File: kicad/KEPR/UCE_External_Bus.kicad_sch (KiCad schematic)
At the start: 5 parts, among them J4 Conn_02x40_Odd_Even, J5 Conn_02x40_Odd_Even, J6 Conn_02x40_Odd_Even, J7 Conn_02x08_Odd_Even, J8 Conn_01x08_Pin

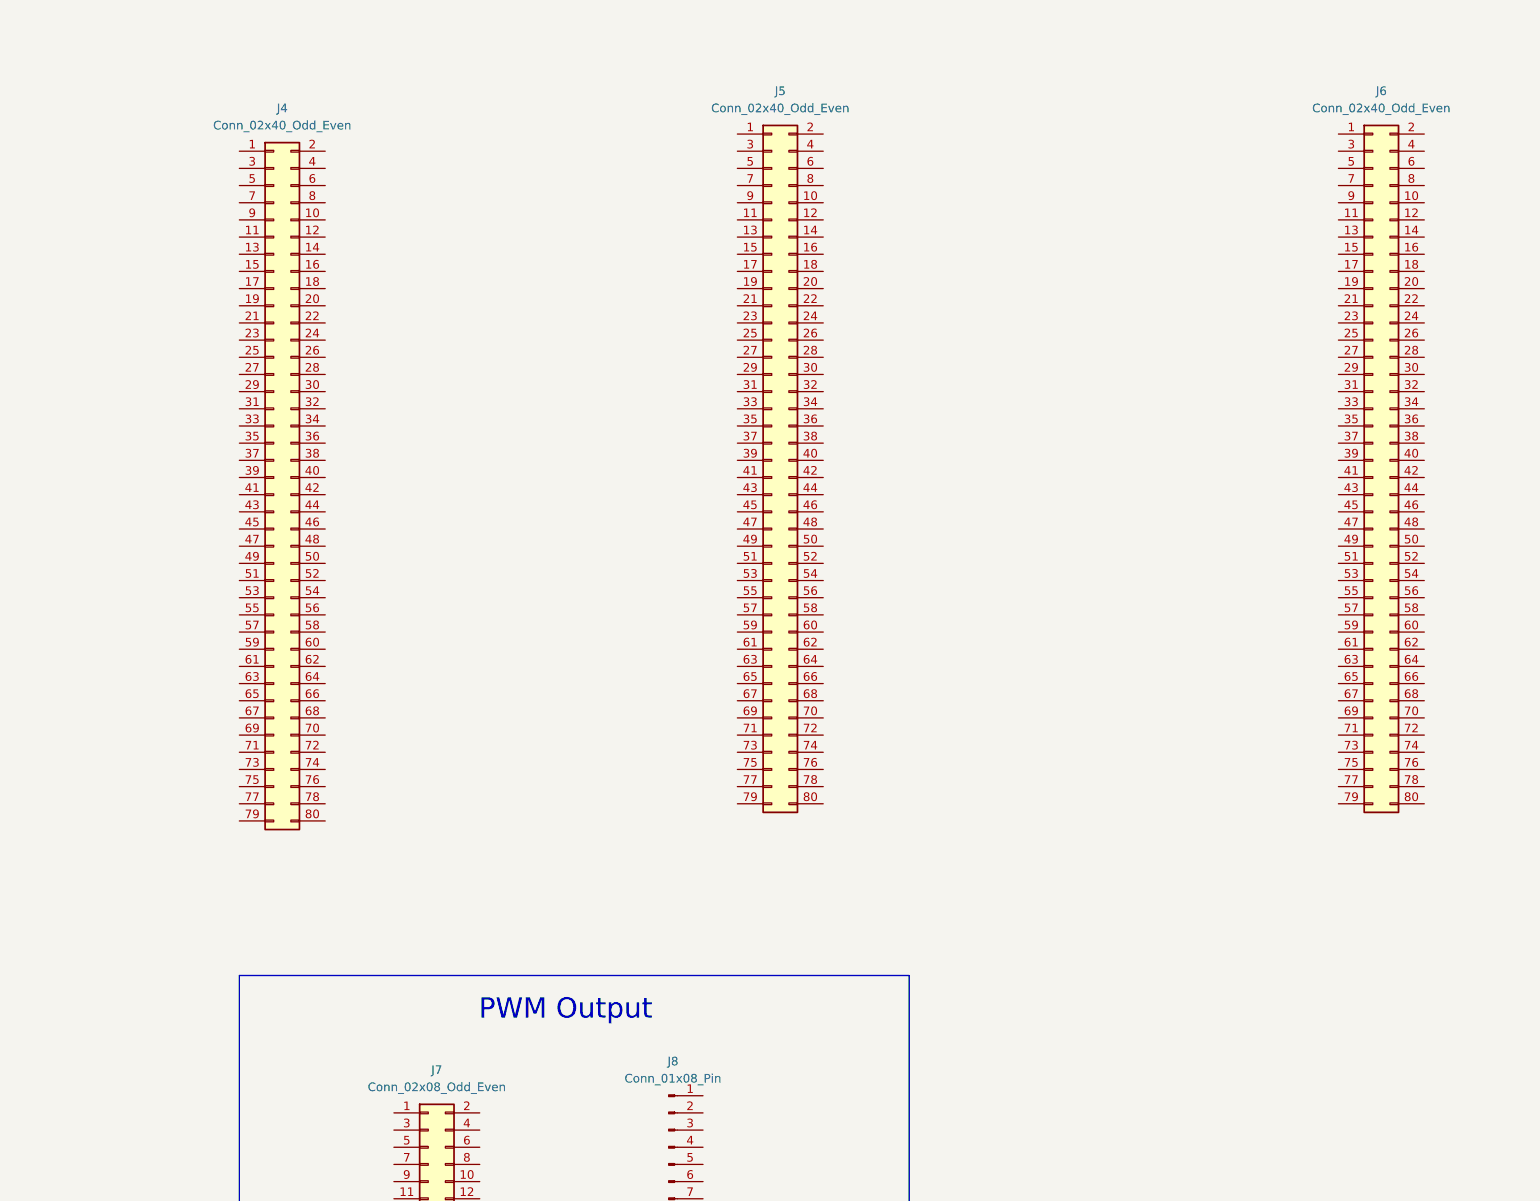
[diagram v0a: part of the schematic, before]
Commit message: Adicinado o barramento externo
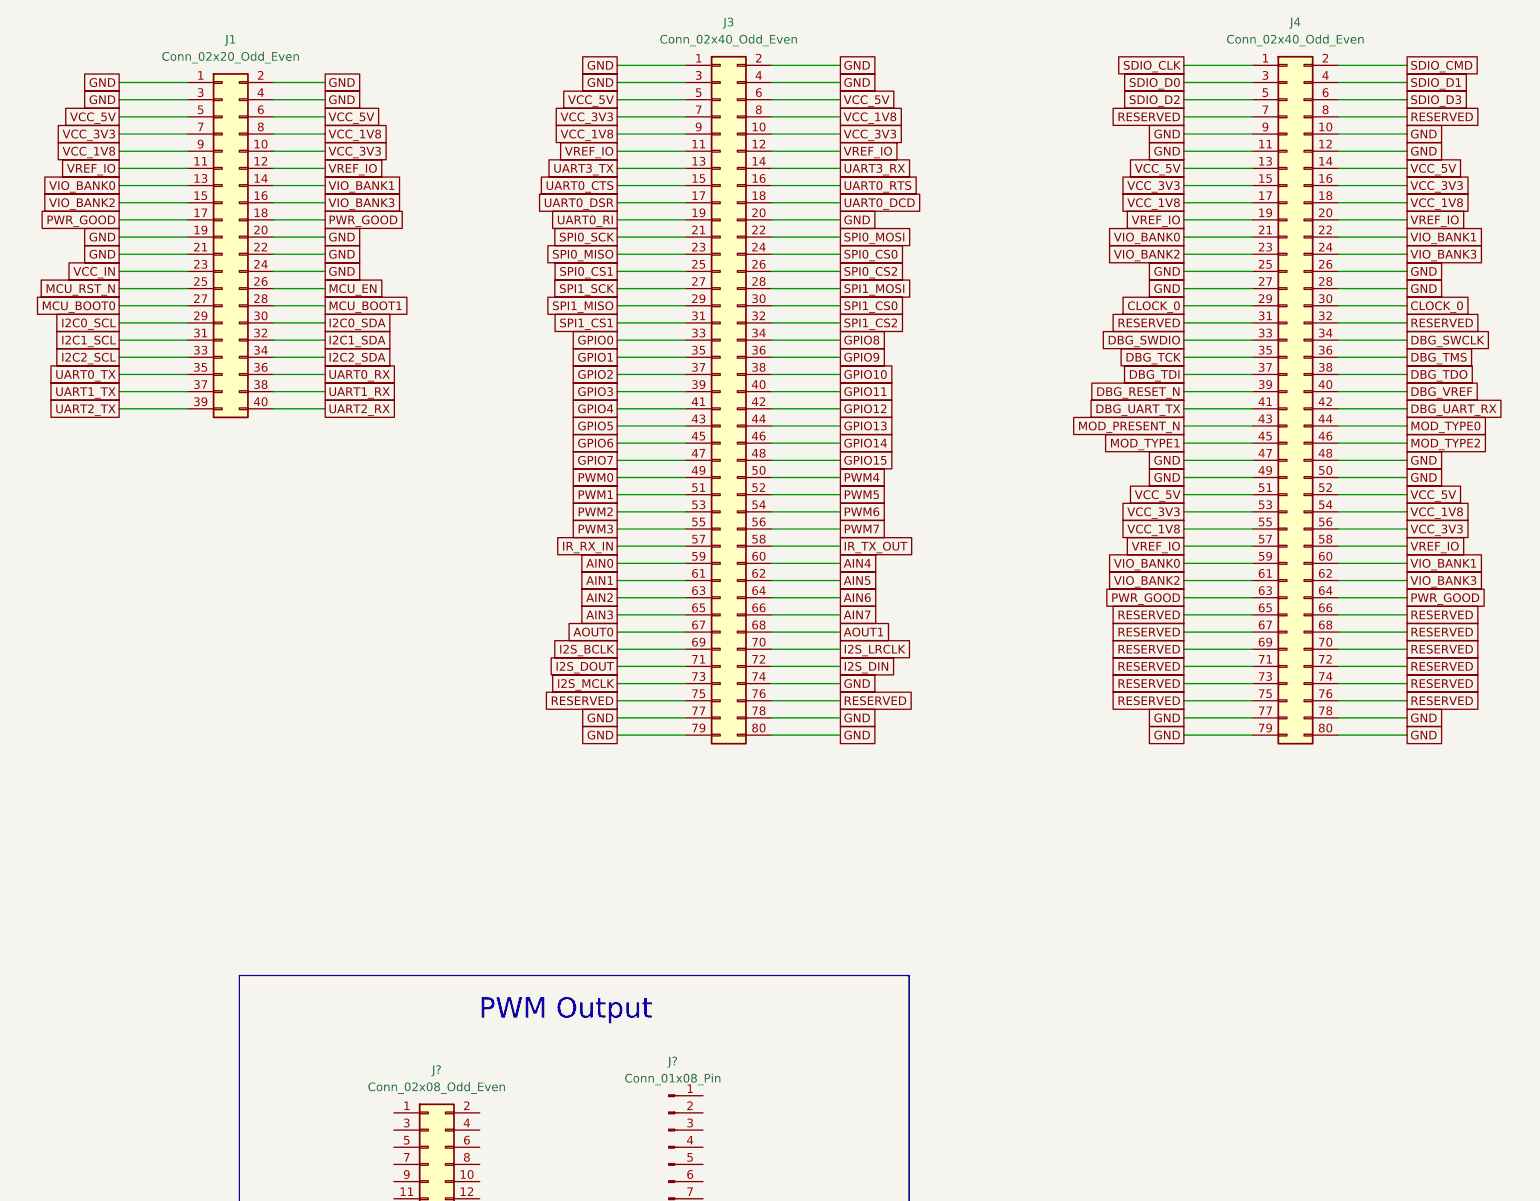
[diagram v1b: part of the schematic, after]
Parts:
- removed J5, J6: Conn_02x40_Odd_Even, symbol Connector_Generic:Conn_02x40_Odd_Even
- added J1: Conn_02x20_Odd_Even, symbol Connector_Generic:Conn_02x20_Odd_Even
- added J3: Conn_02x40_Odd_Even, symbol Connector_Generic:Conn_02x40_Odd_Even
- renumbered J8 to J?, J7 to J?
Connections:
- net SDIO_CLK: now reaches J4.1 (Pin_1)
- net GND: now reaches J4.10 (Pin_10)
- net GND: now also J4.11 (Pin_11), J4.12 (Pin_12), J4.25 (Pin_25), J4.26 (Pin_26), J4.27 (Pin_27), J4.28 (Pin_28), J4.47 (Pin_47), J4.48 (Pin_48), J4.49 (Pin_49), J4.50 (Pin_50), J4.77 (Pin_77), J4.78 (Pin_78), J4.79 (Pin_79), J4.80 (Pin_80), J4.9 (Pin_9), J1.1 (Pin_1), J1.19 (Pin_19), J1.2 (Pin_2), J1.20 (Pin_20), J1.21 (Pin_21), J1.22 (Pin_22), J1.24 (Pin_24), J1.3 (Pin_3), J1.4 (Pin_4), J3.1 (Pin_1), J3.2 (Pin_2), J3.20 (Pin_20), J3.3 (Pin_3), J3.4 (Pin_4), J3.74 (Pin_74), J3.77 (Pin_77), J3.78 (Pin_78), J3.79 (Pin_79), J3.80 (Pin_80)
- net VCC_5V: now reaches J4.13 (Pin_13)
- net VCC_5V: now also J4.14 (Pin_14), J4.51 (Pin_51), J4.52 (Pin_52), J1.5 (Pin_5), J1.6 (Pin_6), J3.5 (Pin_5), J3.6 (Pin_6)
- net VCC_3V3: now reaches J4.15 (Pin_15)
- net VCC_3V3: now also J4.16 (Pin_16), J4.53 (Pin_53), J4.56 (Pin_56), J1.10 (Pin_10), J1.7 (Pin_7), J3.10 (Pin_10), J3.7 (Pin_7)
- net VCC_1V8: now reaches J4.17 (Pin_17)
- net VCC_1V8: now also J4.18 (Pin_18), J4.54 (Pin_54), J4.55 (Pin_55), J1.8 (Pin_8), J1.9 (Pin_9), J3.8 (Pin_8), J3.9 (Pin_9)
- net VREF_IO: now reaches J4.19 (Pin_19)
- net VREF_IO: now also J4.20 (Pin_20), J4.57 (Pin_57), J4.58 (Pin_58), J1.11 (Pin_11), J1.12 (Pin_12), J3.11 (Pin_11), J3.12 (Pin_12)
- net SDIO_CMD: now reaches J4.2 (Pin_2)
- net VIO_BANK0: now reaches J4.21 (Pin_21)
- net VIO_BANK0: now also J4.59 (Pin_59), J1.13 (Pin_13)
- net VIO_BANK1: now reaches J4.22 (Pin_22)
- net VIO_BANK1: now also J4.60 (Pin_60), J1.14 (Pin_14)
- net VIO_BANK2: now reaches J4.23 (Pin_23)
- net VIO_BANK2: now also J4.61 (Pin_61), J1.15 (Pin_15)
- net VIO_BANK3: now reaches J4.24 (Pin_24)
- net VIO_BANK3: now also J4.62 (Pin_62), J1.16 (Pin_16)
- net CLOCK_0: now reaches J4.29 (Pin_29)
- net CLOCK_0: now also J4.30 (Pin_30)
- net SDIO_D0: now reaches J4.3 (Pin_3)
- net RESERVED: now reaches J4.31 (Pin_31)
- net RESERVED: now also J4.32 (Pin_32), J4.65 (Pin_65), J4.66 (Pin_66), J4.67 (Pin_67), J4.68 (Pin_68), J4.69 (Pin_69), J4.7 (Pin_7), J4.70 (Pin_70), J4.71 (Pin_71), J4.72 (Pin_72), J4.73 (Pin_73), J4.74 (Pin_74), J4.75 (Pin_75), J4.76 (Pin_76), J4.8 (Pin_8), J3.75 (Pin_75), J3.76 (Pin_76)
- net DBG_SWDIO: now reaches J4.33 (Pin_33)
- net DBG_SWCLK: now reaches J4.34 (Pin_34)
- net DBG_TCK: now reaches J4.35 (Pin_35)
- net DBG_TMS: now reaches J4.36 (Pin_36)
- net DBG_TDI: now reaches J4.37 (Pin_37)
- net DBG_TDO: now reaches J4.38 (Pin_38)
- net DBG_RESET_N: now reaches J4.39 (Pin_39)
- net SDIO_D1: now reaches J4.4 (Pin_4)
- net DBG_VREF: now reaches J4.40 (Pin_40)
- net DBG_UART_TX: now reaches J4.41 (Pin_41)
- net DBG_UART_RX: now reaches J4.42 (Pin_42)
- net MOD_PRESENT_N: now reaches J4.43 (Pin_43)
- net MOD_TYPE0: now reaches J4.44 (Pin_44)
- net MOD_TYPE1: now reaches J4.45 (Pin_45)
- net MOD_TYPE2: now reaches J4.46 (Pin_46)
- net SDIO_D2: now reaches J4.5 (Pin_5)
- net SDIO_D3: now reaches J4.6 (Pin_6)
- net PWR_GOOD: now reaches J4.63 (Pin_63)
- net PWR_GOOD: now also J4.64 (Pin_64), J1.17 (Pin_17), J1.18 (Pin_18)
- new net AIN0: J3.59 (Pin_59)
- new net AIN1: J3.61 (Pin_61)
- new net AIN2: J3.63 (Pin_63)
- new net AIN3: J3.65 (Pin_65)
- new net AIN4: J3.60 (Pin_60)
- new net AIN5: J3.62 (Pin_62)
- new net AIN6: J3.64 (Pin_64)
- new net AIN7: J3.66 (Pin_66)
- new net AOUT0: J3.67 (Pin_67)
- new net AOUT1: J3.68 (Pin_68)
- new net GPIO0: J3.33 (Pin_33)
- new net GPIO1: J3.35 (Pin_35)
- new net GPIO10: J3.38 (Pin_38)
- new net GPIO11: J3.40 (Pin_40)
- new net GPIO12: J3.42 (Pin_42)
- new net GPIO13: J3.44 (Pin_44)
- new net GPIO14: J3.46 (Pin_46)
- new net GPIO15: J3.48 (Pin_48)
- new net GPIO2: J3.37 (Pin_37)
- new net GPIO3: J3.39 (Pin_39)
- new net GPIO4: J3.41 (Pin_41)
- new net GPIO5: J3.43 (Pin_43)
- new net GPIO6: J3.45 (Pin_45)
- new net GPIO7: J3.47 (Pin_47)
- new net GPIO8: J3.34 (Pin_34)
- new net GPIO9: J3.36 (Pin_36)
- new net I2C0_SCL: J1.29 (Pin_29)
- new net I2C0_SDA: J1.30 (Pin_30)
- new net I2C1_SCL: J1.31 (Pin_31)
- new net I2C1_SDA: J1.32 (Pin_32)
- new net I2C2_SCL: J1.33 (Pin_33)
- new net I2C2_SDA: J1.34 (Pin_34)
- new net I2S_BCLK: J3.69 (Pin_69)
- new net I2S_DIN: J3.72 (Pin_72)
- new net I2S_DOUT: J3.71 (Pin_71)
- new net I2S_LRCLK: J3.70 (Pin_70)
- new net I2S_MCLK: J3.73 (Pin_73)
- new net IR_RX_IN: J3.57 (Pin_57)
- new net IR_TX_OUT: J3.58 (Pin_58)
- new net MCU_BOOT0: J1.27 (Pin_27)
- new net MCU_BOOT1: J1.28 (Pin_28)
- new net MCU_EN: J1.26 (Pin_26)
- new net MCU_RST_N: J1.25 (Pin_25)
- new net PWM0: J3.49 (Pin_49)
- new net PWM1: J3.51 (Pin_51)
- new net PWM2: J3.53 (Pin_53)
- new net PWM3: J3.55 (Pin_55)
- new net PWM4: J3.50 (Pin_50)
- new net PWM5: J3.52 (Pin_52)
- new net PWM6: J3.54 (Pin_54)
- new net PWM7: J3.56 (Pin_56)
- new net SPI0_CS0: J3.24 (Pin_24)
- new net SPI0_CS1: J3.25 (Pin_25)
- new net SPI0_CS2: J3.26 (Pin_26)
- new net SPI0_MISO: J3.23 (Pin_23)
- new net SPI0_MOSI: J3.22 (Pin_22)
- new net SPI0_SCK: J3.21 (Pin_21)
- new net SPI1_CS0: J3.30 (Pin_30)
- new net SPI1_CS1: J3.31 (Pin_31)
- new net SPI1_CS2: J3.32 (Pin_32)
- new net SPI1_MISO: J3.29 (Pin_29)
- new net SPI1_MOSI: J3.28 (Pin_28)
- new net SPI1_SCK: J3.27 (Pin_27)
- new net UART0_CTS: J3.15 (Pin_15)
- new net UART0_DCD: J3.18 (Pin_18)
- new net UART0_DSR: J3.17 (Pin_17)
- new net UART0_RI: J3.19 (Pin_19)
- new net UART0_RTS: J3.16 (Pin_16)
- new net UART0_RX: J1.36 (Pin_36)
- new net UART0_TX: J1.35 (Pin_35)
- new net UART1_RX: J1.38 (Pin_38)
- new net UART1_TX: J1.37 (Pin_37)
- new net UART2_RX: J1.40 (Pin_40)
- new net UART2_TX: J1.39 (Pin_39)
- new net UART3_RX: J3.14 (Pin_14)
- new net UART3_TX: J3.13 (Pin_13)
- new net VCC_IN: J1.23 (Pin_23)

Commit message: Iniciado projeto da PCB, para uma referência de tamanho.
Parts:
- J10: renamed from J4; footprint (none) -> Connector_PinHeader_2.54mm:PinHeader_2x40_P2.54mm_Vertical
- J6: renamed from J1; footprint (none) -> Connector_PinHeader_2.54mm:PinHeader_2x20_P2.54mm_Vertical
- J9: renamed from J3; footprint (none) -> Connector_PinHeader_2.54mm:PinHeader_2x40_P2.54mm_Vertical
- gave numbers to parts that had none: 2
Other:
- note added: "## 2. Convenções e Domínios Elétricos ### 2.1 Domínios de alimentação Os seguintes domínios aparecem na especificação do UCE e são utilizados/propagados no barramento: - `VCC_5V` - `VCC_3V3` - `VCC_1V8` - `GND` ### 2.2 Referência e níveis lógicos - `VREF_IO`: referência de IO (associada ao domínio lógico exposto). - `VIO_BANK0`, `VIO_BANK1`, `VIO_BANK2`, `VIO_BANK3`: tensões por banco de IO, alin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"
- moved on the sheet: J7, J8
